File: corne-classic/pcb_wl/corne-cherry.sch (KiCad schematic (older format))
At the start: 72 parts, among them J1 MJ-4PP-9, J2 OLED, J3 Conn_01x02_Female, SW1 SW_PUSH, SW10 SW_PUSH, SW11 SW_PUSH, SW12 SW_PUSH, SW13 SW_PUSH, SW14 SW_PUSH, SW15 SW_PUSH, SW16 SW_PUSH, SW17 SW_PUSH, SW18 SW_PUSH, SW19 SW_PUSH, SW2 SW_PUSH, SW20 SW_PUSH, SW21 SW_PUSH, SW22 SW_PUSH, SW23 SW_SPDT, SW24 SW_SPDT, SW3 SW_PUSH, SW4 SW_PUSH, SW5 SW_PUSH, SW6 SW_PUSH, SW7 SW_PUSH, SW8 SW_PUSH, SW9 SW_PUSH, U1 ProMicro

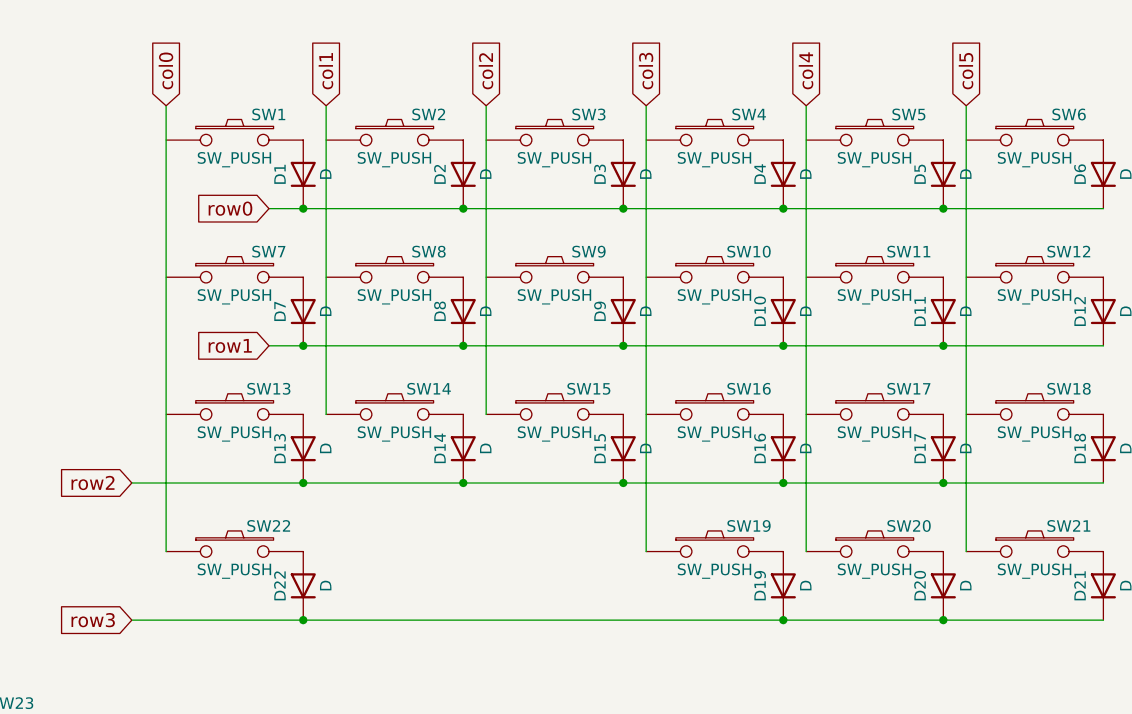
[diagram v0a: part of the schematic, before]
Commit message: Added Alps support and invertible SI thumbs
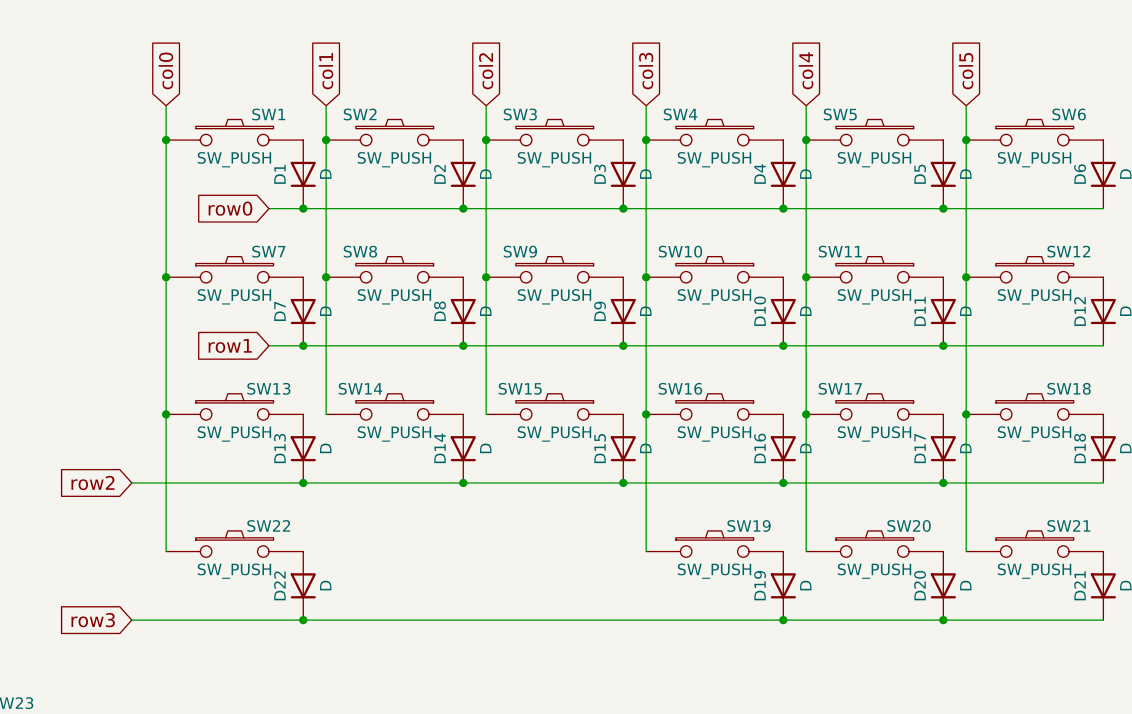
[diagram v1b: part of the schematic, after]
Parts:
- G1, G2: footprint Silks:sporne-logo-small -> sporne:sporne-logo-small
- J3: footprint kbd:Battery_Header -> sporne:Battery_Header
- SW1, SW10, SW11, SW12, SW13, SW14, SW15, SW16, SW17, SW18, SW2, SW22, SW3, SW4, SW5, SW6, SW7, SW8, SW9: footprint kbd:MX_Hitek_725_1U_reversible -> sporne:MX_Alps_Hitek_725_1U_reversible
- SW19, SW20: footprint kbd:MX_Hitek_725_1U_reversible -> sporne:MX_Alps_Hitek_725_1U_reversible_thumb
- SW21: footprint kbd:MX_Hitek_725_1.5U_reversible -> sporne:MX_Alps_Hitek_725_1.5U_reversible_thumb
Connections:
- net col0: now also SW1.1, SW13.1, SW7.1
- net col1: now also SW14.2, SW2.2, SW8.2; no longer SW14.1
- net col2: now also SW15.2, SW3.2, SW9.2; no longer SW15.1
- net col3: now also SW10.2, SW16.2, SW4.2
- net col4: now also SW11.2, SW17.2, SW5.2
- net col5: now also SW12.1, SW18.1, SW6.1
- net at SW2.1: now also D2.2 (A)
- net at SW3.1: now also D3.2 (A)
- net at SW4.1: now also D4.2 (A)
- net at SW5.1: now also D5.2 (A)
- net at SW8.1: now also D8.2 (A)
- net at SW9.1: now also D9.2 (A)
- net at SW10.1: now also D10.2 (A)
- net at SW11.1: now also D11.2 (A)
- net at D14.2 (A): now also SW14.1; no longer SW14.2
- net at D15.2 (A): now also SW15.1; no longer SW15.2
- net at SW16.1: now also D16.2 (A)
- net at SW17.1: now also D17.2 (A)
